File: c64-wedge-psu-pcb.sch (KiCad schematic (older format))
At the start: 16 parts, among them U1 LM2576T-5

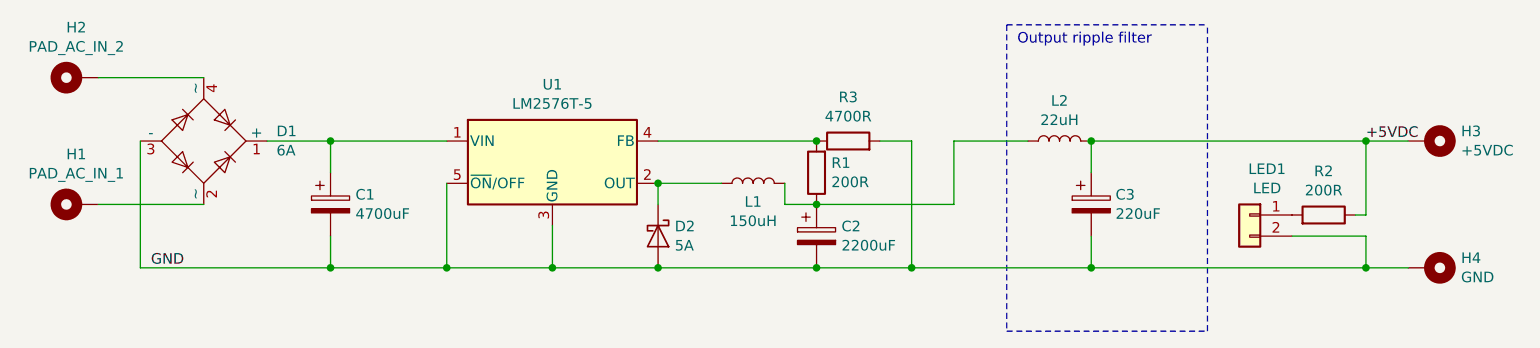
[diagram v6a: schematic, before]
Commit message: Adjust feedback voltage divider resitor values. Reposition led resistor, there is no room in previous position. Minor layout changes.
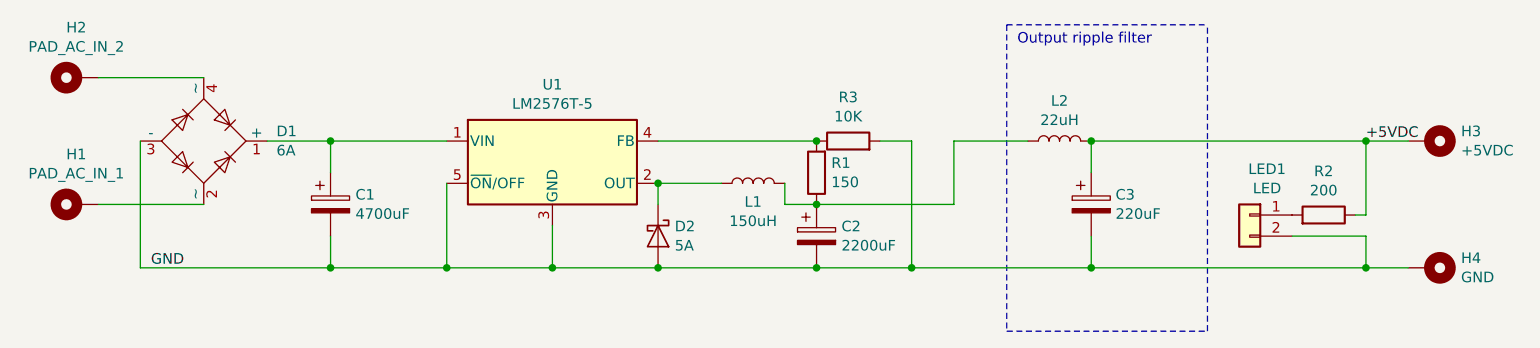
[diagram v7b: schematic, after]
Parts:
- R1: value 200R -> 150
- R2: value 200R -> 200
- R3: value 4700R -> 10K
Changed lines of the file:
@@
 Sheet 1 1
 Title "C64 Wedge PSU PCB"
-Date "2022-01-30"
-Rev "1.2"
+Date "2022-06-08"
+Rev "1.3"
 Comp "Timo Mömmö"
 Comment1 ""
@@
 P 8250 4000
 F 0 "R2" V 8457 4000 50  0000 C CNN
-F 1 "200R" V 8366 4000 50  0000 C CNN
+F 1 "200" V 8366 4000 50  0000 C CNN
 F 2 "Resistor_THT:R_Axial_DIN0207_L6.3mm_D2.5mm_P7.62mm_Horizontal" V 8180 4000 50  0001 C CNN
 F 3 "~" H 8250 4000 50  0001 C CNN
@@
 P 5850 3800
 F 0 "R1" H 5780 3754 50  0000 R CNN
-F 1 "200R" H 5780 3845 50  0000 R CNN
+F 1 "150" H 5780 3845 50  0000 R CNN
 F 2 "Resistor_THT:R_Axial_DIN0207_L6.3mm_D2.5mm_P7.62mm_Horizontal" V 5780 3800 50  0001 C CNN
 F 3 "~" H 5850 3800 50  0001 C CNN
@@
 P 6000 3650
 F 0 "R3" V 6207 3650 50  0000 C CNN
-F 1 "4700R" V 6116 3650 50  0000 C CNN
+F 1 "10K" V 6116 3650 50  0000 C CNN
 F 2 "Resistor_THT:R_Axial_DIN0207_L6.3mm_D2.5mm_P7.62mm_Horizontal" V 5930 3650 50  0001 C CNN
 F 3 "~" H 6000 3650 50  0001 C CNN
